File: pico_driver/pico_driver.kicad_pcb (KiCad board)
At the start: 4 copper layers, 65 x 56 mm, 25 parts, among them J1 GPIO, J2 SRV, J3 ESC, J4 ADC, J5 GP_Breakout, J6 VBUS_OUT, J7 3V3_OUT, J8 FUNC, SW1 SW_SPDT, SW2 SW_Push, SW3 SW_Push, U1 Pico

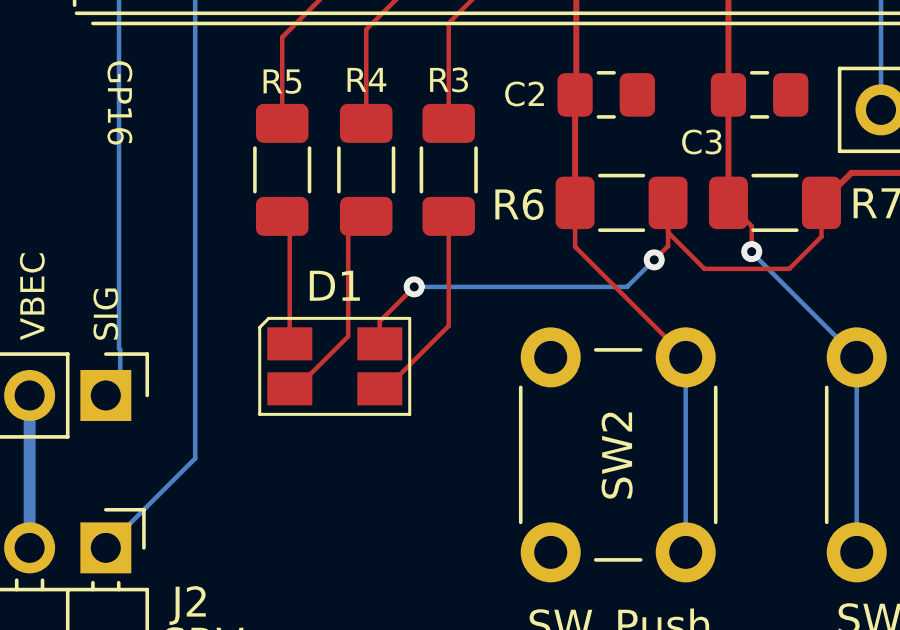
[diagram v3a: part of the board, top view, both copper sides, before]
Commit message: update rgb led footprint and layout
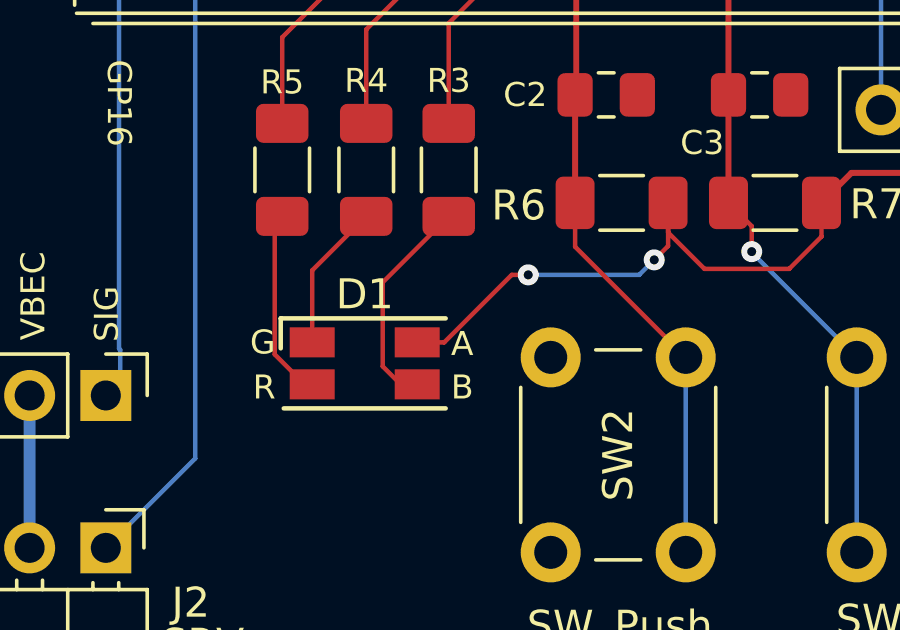
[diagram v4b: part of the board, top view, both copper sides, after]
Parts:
- D1: value ASMB-MTB1-0A3A2 -> LED_GRBA; footprint LED_SMD:LED_Avago_PLCC4_3.2x2.8mm_CW -> LED_SMD:LED_RGB_1210
- moved D1 1.00 mm to (123.0, 89.3)
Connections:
- D1 pad 1: Net-(D1-RK) -> Net-(D1-GK)
- D1 pad 2: Net-(D1-GK) -> Net-(D1-RK)
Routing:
- net Net-(D1-RK): track 4.35 -> 6.37 mm
- net Net-(D1-GK): track 6.92 -> 4.95 mm
- net 3V3_OUT: track 43.4 -> 41.7 mm
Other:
- board text added: "A"
- board text added: "B"
- board text added: "G"
- board text added: "R"
